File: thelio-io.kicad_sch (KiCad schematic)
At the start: 24 parts, among them Y1 16MHz

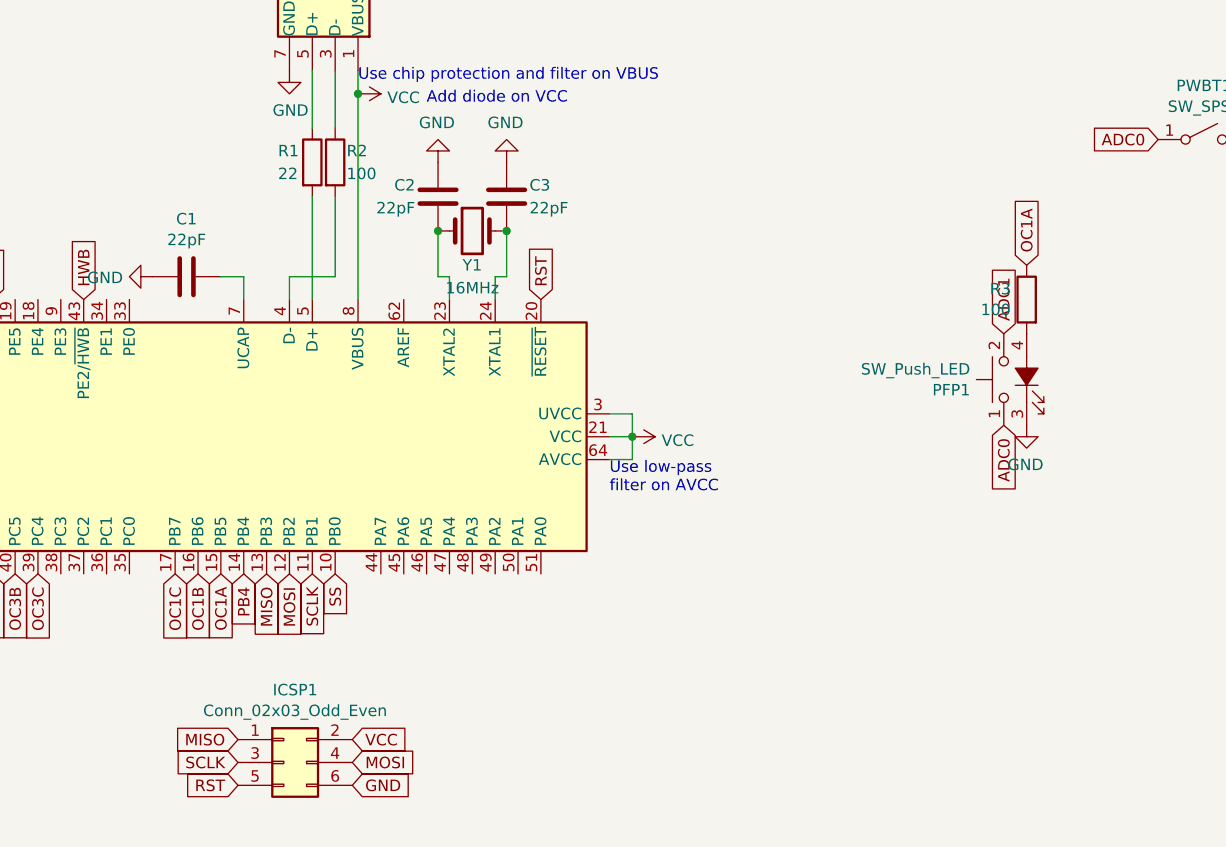
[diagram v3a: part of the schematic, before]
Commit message: decoupling, etc add 3x 1 uF decoupling caps change UCAP from 22 pF to 1 uF as required by AVR datasheet R3 0201 to 0603 package R2 100 to 22 ohm add part number for crystal move VCC planelet to In1.Cu, make In2.Cu solid plane layer swap some traces to allow for planes move power, ground vias closer to IC pins
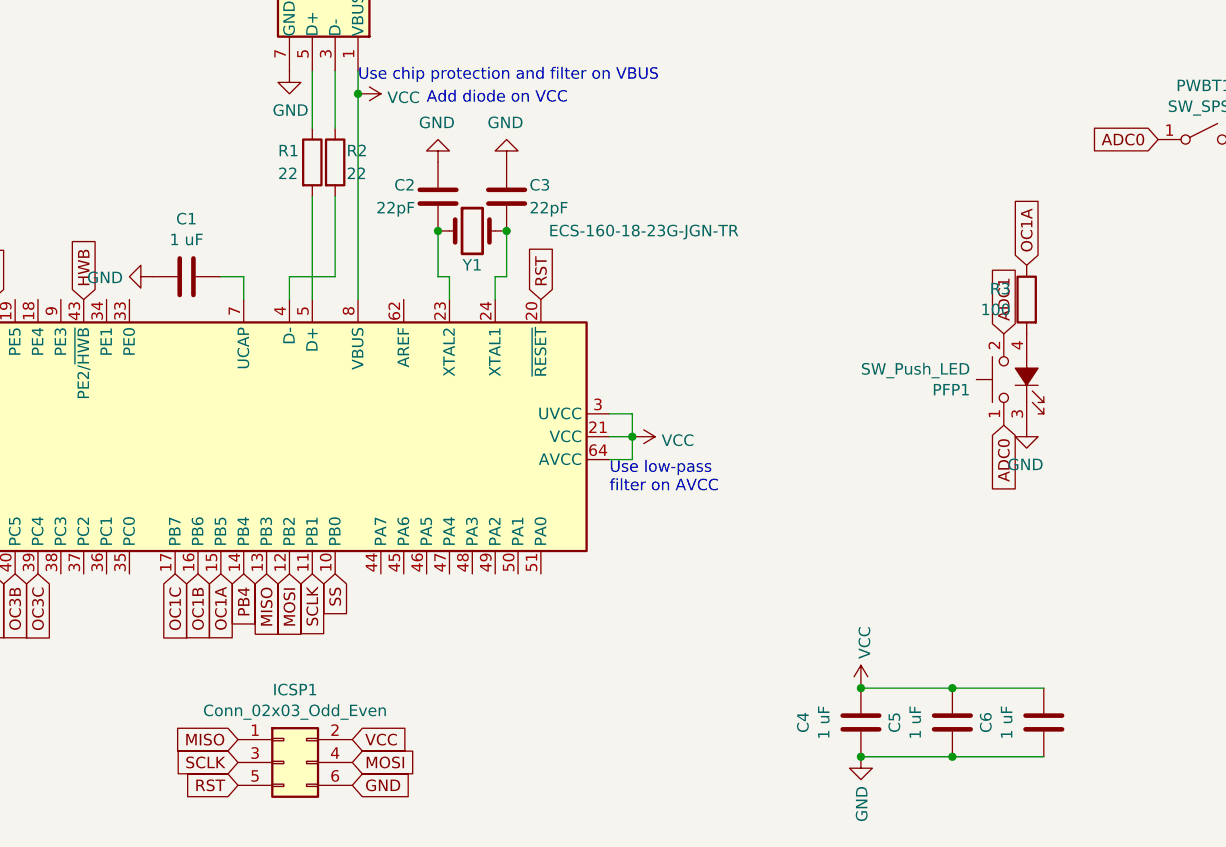
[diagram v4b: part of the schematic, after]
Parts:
- added C4, C5, C6: 1 uF, Capacitor_SMD:C_0402_1005Metric, symbol Device:C
- C1: value 22pF -> 1 uF
- R2: value 100 -> 22
- R3: footprint Resistor_SMD:R_0201_0603Metric -> Resistor_SMD:R_0603_1608Metric
- Y1: value 16MHz -> ECS-160-18-23G-JGN-TR
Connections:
- net GND: now also C4.2, C5.2, C6.2
- net VCC: now also C4.1, C5.1, C6.1
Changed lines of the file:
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@@
 (kicad_sch (version 20211123) (generator eeschema)
   (paper "A4")
+  (junction (at 172.72 154.94) (diameter 0) (color 0 0 0 0)
+  )
+  (junction (at 172.72 147.32) (diameter 0) (color 0 0 0 0)
+  )
   (junction (at 133.35 96.52) (diameter 0) (color 0 0 0 0)
   )
@@
   (junction (at 125.73 96.52) (diameter 0) (color 0 0 0 0)
   )
+  (junction (at 182.88 154.94) (diameter 0) (color 0 0 0 0)
+  )
+  (junction (at 182.88 147.32) (diameter 0) (color 0 0 0 0)
+  )
   (wire (pts (xy 104.14 104.14) (xy 104.14 101.6))
     (stroke (width 0) (type default) (color 0 0 0 0))
@@
     (stroke (width 0) (type default) (color 0 0 0 0))
   )
+  (wire (pts (xy 172.72 154.94) (xy 182.88 154.94))
+    (stroke (width 0) (type default) (color 0 0 0 0))
+  )
+  (wire (pts (xy 182.88 147.32) (xy 193.04 147.32))
+    (stroke (width 0) (type default) (color 0 0 0 0))
+  )
   (wire (pts (xy 111.76 92.71) (xy 111.76 104.14))
     (stroke (width 0) (type default) (color 0 0 0 0))
   )
+  (wire (pts (xy 172.72 147.32) (xy 182.88 147.32))
+    (stroke (width 0) (type default) (color 0 0 0 0))
+  )
   (wire (pts (xy 147.32 119.38) (xy 147.32 121.92))
     (stroke (width 0) (type default) (color 0 0 0 0))
@@
   )
   (wire (pts (xy 144.78 119.38) (xy 147.32 119.38))
+    (stroke (width 0) (type default) (color 0 0 0 0))
+  )
+  (wire (pts (xy 182.88 154.94) (xy 193.04 154.94))
     (stroke (width 0) (type default) (color 0 0 0 0))
   )
@@
     (pin "7")
     (pin "8")
+  )
+  (symbol (lib_id "power:GND") (at 172.72 154.94 0) (unit 1)
+    (in_bom yes) (on_board yes)
+    (property "Reference" "#PWR0101" (id 0) (at 172.72 161.29 0)
+      (effects (font (size 1.27 1.27)) hide)
+    )
+    (property "Value" "GND" (id 1) (at 172.847 158.1912 90)
+      (effects (font (size 1.27 1.27)) (justify right))
+    )
+    (property "Footprint" "" (id 2) (at 172.72 154.94 0)
+      (effects (font (size 1.27 1.27)) hide)
+    )
+    (property "Datasheet" "" (id 3) (at 172.72 154.94 0)
+      (effects (font (size 1.27 1.27)) hide)
+    )
+    (pin "1")
   )
   (symbol (lib_id "power:+12V") (at 266.065 54.61 270) (unit 1)
@@
     (pin "1")
   )
+  (symbol (lib_id "Device:C") (at 193.04 151.13 0) (unit 1)
+    (in_bom yes) (on_board yes)
+    (property "Reference" "C6" (id 0) (at 186.6392 151.13 90))
+    (property "Value" "1 uF" (id 1) (at 188.9506 151.13 90))
+    (property "Footprint" "Capacitor_SMD:C_0402_1005Metric" (id 2) (at 194.0052 154.94 0)
+      (effects (font (size 1.27 1.27)) hide)
+    )
+    (property "Datasheet" "~" (id 3) (at 193.04 151.13 0)
+      (effects (font (size 1.27 1.27)) hide)
+    )
+    (pin "1")
+    (pin "2")
+  )
   (symbol (lib_id "Connector_Generic:Conn_02x03_Odd_Even") (at 108.585 155.575 0) (unit 1)
     (in_bom yes) (on_board yes)
@@
       (effects (font (size 1.27 1.27)) (justify left))
     )
-    (property "Value" "100" (id 1) (at 115.57 90.17 0)
+    (property "Value" "22" (id 1) (at 115.57 90.17 0)
       (effects (font (size 1.27 1.27)) (justify left))
     )
@@
     (in_bom yes) (on_board yes)
     (property "Reference" "C1" (id 0) (at 97.79 95.1992 90))
-    (property "Value" "22pF" (id 1) (at 97.79 97.5106 90))
+    (property "Value" "1 uF" (id 1) (at 97.79 97.5106 90))
     (property "Footprint" "Capacitor_SMD:C_0402_1005Metric" (id 2) (at 93.98 102.5652 0)
       (effects (font (size 1.27 1.27)) hide)
@@
     (pin "2")
   )
+  (symbol (lib_id "power:VCC") (at 172.72 147.32 0) (unit 1)
+    (in_bom yes) (on_board yes)
+    (property "Reference" "#PWR0102" (id 0) (at 172.72 151.13 0)
+      (effects (font (size 1.27 1.27)) hide)
+    )
+    (property "Value" "VCC" (id 1) (at 173.1518 144.0688 90)
+      (effects (font (size 1.27 1.27)) (justify left))
+    )
+    (property "Footprint" "" (id 2) (at 172.72 147.32 0)
+      (effects (font (size 1.27 1.27)) hide)
+    )
+    (property "Datasheet" "" (id 3) (at 172.72 147.32 0)
+      (effects (font (size 1.27 1.27)) hide)
+    )
+    (pin "1")
+  )
+  (symbol (lib_id "Device:C") (at 172.72 151.13 0) (unit 1)
+    (in_bom yes) (on_board yes)
+    (property "Reference" "C4" (id 0) (at 166.3192 151.13 90))
+    (property "Value" "1 uF" (id 1) (at 168.6306 151.13 90))
+    (property "Footprint" "Capacitor_SMD:C_0402_1005Metric" (id 2) (at 173.6852 154.94 0)
+      (effects (font (size 1.27 1.27)) hide)
+    )
+    (property "Datasheet" "~" (id 3) (at 172.72 151.13 0)
+      (effects (font (size 1.27 1.27)) hide)
+    )
+    (pin "1")
+    (pin "2")
+  )
   (symbol (lib_id "Device:R") (at 191.135 104.14 0) (mirror y) (unit 1)
     (in_bom yes) (on_board yes)
@@
       (effects (font (size 1.27 1.27)) (justify left))
     )
-    (property "Footprint" "Resistor_SMD:R_0201_0603Metric" (id 2) (at 192.913 104.14 90)
+    (property "Footprint" "Resistor_SMD:R_0603_1608Metric" (id 2) (at 192.913 104.14 90)
       (effects (font (size 1.27 1.27)) hide)
     )
@@
     (in_bom yes) (on_board yes)
     (property "Reference" "Y1" (id 0) (at 129.54 100.33 0))
-    (property "Value" "16MHz" (id 1) (at 129.54 102.87 0))
+    (property "Value" "ECS-160-18-23G-JGN-TR" (id 1) (at 148.59 96.52 0))
     (property "Footprint" "Crystal:Crystal_SMD_0603-2Pin_6.0x3.5mm" (id 2) (at 129.54 96.52 0)
       (effects (font (size 1.27 1.27)) hide)
     )
     (property "Datasheet" "~" (id 3) (at 129.54 96.52 0)
+      (effects (font (size 1.27 1.27)) hide)
+    )
+    (pin "1")
+    (pin "2")
+  )
+  (symbol (lib_id "Device:C") (at 182.88 151.13 0) (unit 1)
+    (in_bom yes) (on_board yes)
+    (property "Reference" "C5" (id 0) (at 176.4792 151.13 90))
+    (property "Value" "1 uF" (id 1) (at 178.7906 151.13 90))
+    (property "Footprint" "Capacitor_SMD:C_0402_1005Metric" (id 2) (at 183.8452 154.94 0)
+      (effects (font (size 1.27 1.27)) hide)
+    )
+    (property "Datasheet" "~" (id 3) (at 182.88 151.13 0)
       (effects (font (size 1.27 1.27)) hide)
     )
@@
       (reference "#PWR023") (unit 1) (value "+12V") (footprint "")
     )
+    (path "/28d843b2-978b-4d39-bd30-26580fa80b83"
+      (reference "#PWR0101") (unit 1) (value "GND") (footprint "")
+    )
+    (path "/a2f6d203-ebeb-4775-ac27-92e1a315ea1f"
+      (reference "#PWR0102") (unit 1) (value "VCC") (footprint "")
+    )
     (path "/3a0f81ba-204f-45e9-83fb-f7bade0d2ad1"
       (reference "AVR1") (unit 1) (value "ATmega32U4-AU") (footprint "Package_DFN_QFN:QFN-64-1EP_9x9mm_P0.5mm_EP7.5x7.5mm")
     )
     (path "/95d7b4e4-d090-4b4b-95d7-0687255342ed"
-      (reference "C1") (unit 1) (value "22pF") (footprint "Capacitor_SMD:C_0402_1005Metric")
+      (reference "C1") (unit 1) (value "1 uF") (footprint "Capacitor_SMD:C_0402_1005Metric")
     )
     (path "/ca6b3c6e-f279-44df-940f-3fcf5357fcd4"
@@
       (reference "C3") (unit 1) (value "22pF") (footprint "Capacitor_SMD:C_0402_1005Metric")
     )
+    (path "/a878a433-44b7-4c70-8fb4-32bc0d732a65"
+      (reference "C4") (unit 1) (value "1 uF") (footprint "Capacitor_SMD:C_0402_1005Metric")
+    )
+    (path "/fc80f10e-2697-49ce-b85e-a5592bbe3889"
+      (reference "C5") (unit 1) (value "1 uF") (footprint "Capacitor_SMD:C_0402_1005Metric")
+    )
+    (path "/519c6cbc-2cef-4756-9976-f1eb263c94ab"
+      (reference "C6") (unit 1) (value "1 uF") (footprint "Capacitor_SMD:C_0402_1005Metric")
+    )
     (path "/684a5de3-a519-44ea-bebe-5a3b8e01f198"
       (reference "F1") (unit 1) (value "3A Fuse") (footprint "Fuse:Fuse_0603_1608Metric")
@@
     )
     (path "/5e98e7b2-f6af-4d33-bd91-1e12cd43a4af"
-      (reference "R2") (unit 1) (value "100") (footprint "Resistor_SMD:R_0603_1608Metric")
+      (reference "R2") (unit 1) (value "22") (footprint "Resistor_SMD:R_0603_1608Metric")
     )
     (path "/a93da457-a261-4a8a-92cf-b2b33bf2aef6"
-      (reference "R3") (unit 1) (value "100") (footprint "Resistor_SMD:R_0201_0603Metric")
+      (reference "R3") (unit 1) (value "100") (footprint "Resistor_SMD:R_0603_1608Metric")
     )
     (path "/24da91e1-4b2d-4e79-a096-b2424715c2dc"
@@
     )
     (path "/ee06c0cd-13b9-4549-a21e-0082e6f6e36d"
-      (reference "Y1") (unit 1) (value "16MHz") (footprint "Crystal:Crystal_SMD_0603-2Pin_6.0x3.5mm")
-    )
-  )
+      (reference "Y1") (unit 1) (value "ECS-160-18-23G-JGN-TR") (footprint "Crystal:Crystal_SMD_0603-2Pin_6.0x3.5mm")
+    )
+  )

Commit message: part numbers, export settings
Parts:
- added C8: 1 uF, Capacitor_SMD:C_0402_1005Metric, symbol Device:C
- AVR1: value ATmega32U4-AU -> AT90USB646-MUR; Manufacturer (none) -> Microchip
- C1, C4, C5, C6, R1, R2, R3: Manufacturer (none) -> generic
- C2, C3: value 22pF -> 22 pF; Manufacturer (none) -> generic
- F1: value 3A Fuse -> FMC16302WBTPCT; Manufacturer (none) -> Kamaya
- FANIN1, FANOUT1, FANOUT2, FANOUT3, FANOUT4: value Fan_Tacho_PWM -> 47053-1000; Manufacturer (none) -> Molex (generic OK)
- ICSP1: value Conn_02x03_Odd_Even -> 54202-S0803LF; Manufacturer (none) -> Amphenol FCI (generic equivalent OK)
- MUX1, MUX2, MUX3, MUX4: value 74LVC2G157 -> SN74LVC2G157DCUR; Manufacturer (none) -> TI
- PFP1, PMB1: value SW_Push_LED -> 22-28-4040; Manufacturer (none) -> Molex (generic OK)
- POWER1: value ATA_FLOPPY_POWER_4 -> 171825-4; Manufacturer (none) -> Molex (generic OK)
- PWBT1: value SW_SPST -> TL3342F260QG; Manufacturer (none) -> E-Switch (generic equivalent OK)
- USB1: value USB_IDC -> header_9_USB; Manufacturer (none) -> generic
- Y1: Manufacturer (none) -> ECS
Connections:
- net HWB is gone; now on net GND: AVR1.43 (PE2/~{HWB})
- net GND: now also MUX1.7 (~{G}), MUX2.7 (~{G}), MUX3.7 (~{G}), MUX4.7 (~{G}), C8.1
- net XTAL2: now reaches AVR1.23 (XTAL2), C2.2, Y1.1
- net XTAL1: now reaches AVR1.24 (XTAL1), C3.2, Y1.2
- net AREF: now reaches AVR1.62 (AREF)
- net AREF: now also C8.2
- net UCAP: now reaches AVR1.7 (UCAP), C1.1
- net OC1B: no longer names the net of AVR1.16 (PB6)
- net PB4: no longer names the net of AVR1.14 (PB4)
- net SS: no longer names the net of AVR1.10 (PB0)
- no-connect marks 0 -> 41
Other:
- note added: "OC1B"
- note added: "SS"
- note removed: "Add diode on VCC"
- note removed: "Use chip protection and filter on VBUS"
- note removed: "Use low-pass filter on AVCC"
- company: (none) -> System76
- title: (none) -> Thelio IO
- moved on the sheet: AVR1, C1, C2, C3, ICSP1, R1, R2, USB1, Y1

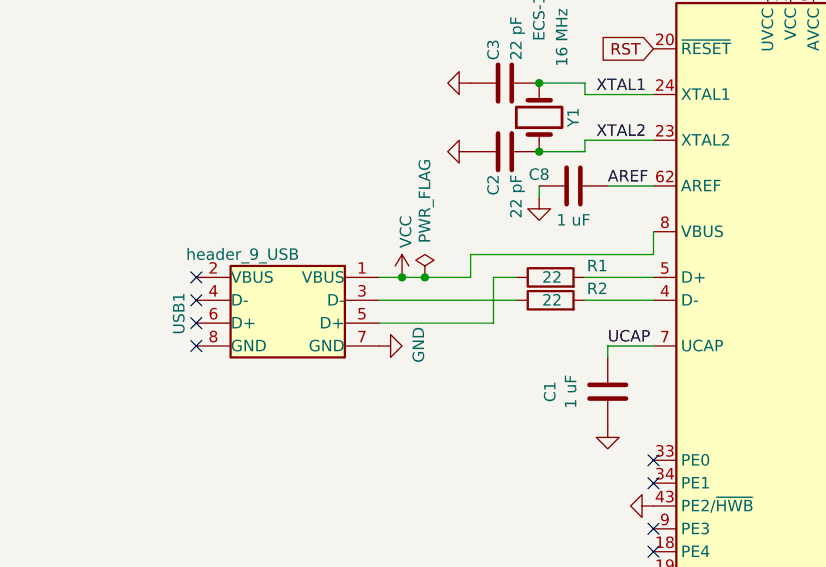
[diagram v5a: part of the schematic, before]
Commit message: change USB connector to Molex SL style
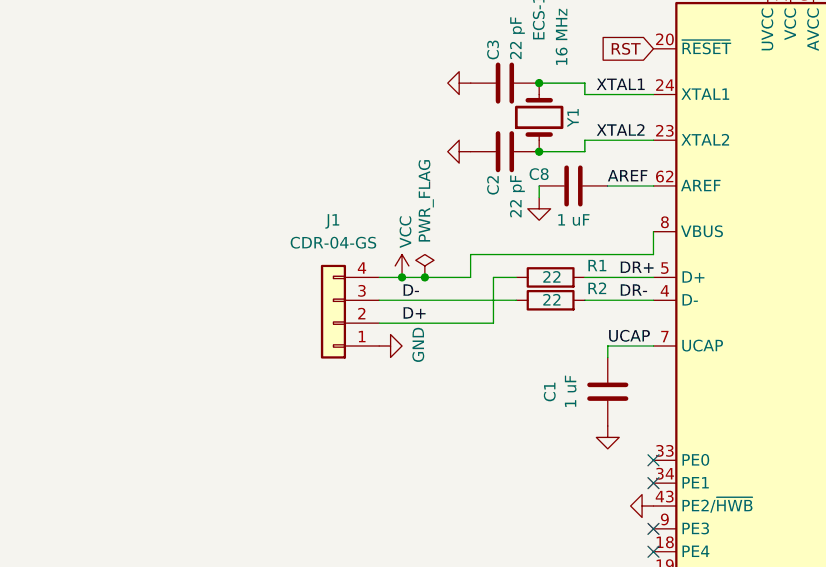
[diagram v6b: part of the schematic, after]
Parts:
- removed USB1: header_9_USB, USB:USB_IDC, symbol USB:USB_IDC
- added J1: CDR-04-GS, Connector_Molex:Molex_SL_171971-0004_1x04_P2.54mm_Vertical, symbol Connector_Generic:Conn_01x04
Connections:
- net GND: now also J1.1 (Pin_1)
- net VCC: now also J1.4 (Pin_4)
- net D+: now reaches R1.1
- net D+: now also J1.2 (Pin_2)
- net DR+: now reaches AVR1.5 (D+), R1.2
- net D-: now reaches R2.1
- net D-: now also J1.3 (Pin_3)
- net DR-: now reaches AVR1.4 (D-), R2.2
- no-connect marks 41 -> 37
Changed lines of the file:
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@@
   )
   (no_connect (at 128.27 91.44))
-  (no_connect (at 46.99 124.46))
   (no_connect (at 128.27 106.68))
   (no_connect (at 128.27 93.98))
@@
   (no_connect (at 158.115 54.61))
   (no_connect (at 128.27 142.24))
-  (no_connect (at 46.99 119.38))
   (no_connect (at 128.27 177.8))
   (no_connect (at 128.27 170.18))
-  (no_connect (at 46.99 116.84))
   (no_connect (at 203.2 39.37))
   (no_connect (at 128.27 124.46))
@@
   (no_connect (at 128.27 109.22))
   (no_connect (at 128.27 101.6))
-  (no_connect (at 46.99 121.92))
   (no_connect (at 128.27 154.94))
   (no_connect (at 128.27 99.06))
@@
     (effects (font (size 1.27 1.27)) (justify right bottom))
   )
+  (label "DR+" (at 93.98 116.84 0)
+    (effects (font (size 1.27 1.27)) (justify left bottom))
+  )
   (label "XTAL2" (at 91.44 101.6 0)
     (effects (font (size 1.27 1.27)) (justify left bottom))
@@
     (effects (font (size 1.27 1.27)) (justify left bottom))
   )
+  (label "DR-" (at 93.98 119.38 0)
+    (effects (font (size 1.27 1.27)) (justify left bottom))
+  )
   (label "XTAL1" (at 91.44 96.52 0)
+    (effects (font (size 1.27 1.27)) (justify left bottom))
+  )
+  (label "D+" (at 69.85 121.92 0)
+    (effects (font (size 1.27 1.27)) (justify left bottom))
+  )
+  (label "D-" (at 69.85 119.38 0)
     (effects (font (size 1.27 1.27)) (justify left bottom))
   )
@@
     )
     (pin "1")
-  )
-  (symbol (lib_id "USB:USB_IDC") (at 62.23 121.92 0) (mirror y) (unit 1)
-    (in_bom yes) (on_board yes)
-    (property "Reference" "USB1" (id 0) (at 45.085 123.19 90)
-      (effects (font (size 1.27 1.27)) (justify left))
-    )
-    (property "Value" "header_9_USB" (id 1) (at 58.42 114.3 0)
-      (effects (font (size 1.27 1.27)) (justify left))
-    )
-    (property "Footprint" "USB:USB_IDC" (id 2) (at 62.23 121.92 0)
-      (effects (font (size 1.27 1.27)) hide)
-    )
-    (property "Datasheet" "~" (id 3) (at 62.23 121.92 0)
-      (effects (font (size 1.27 1.27)) hide)
-    )
-    (property "Description" "10 pin shrouded 2x5 2.54 mm pitch header with pin 9 removed" (id 4) (at 62.23 121.92 0)
-      (effects (font (size 1.27 1.27)) hide)
-    )
-    (property "Manufacturer" "generic" (id 5) (at 62.23 121.92 0)
-      (effects (font (size 1.27 1.27)) hide)
-    )
-    (pin "1")
-    (pin "2")
-    (pin "3")
-    (pin "4")
-    (pin "5")
-    (pin "6")
-    (pin "7")
-    (pin "8")
   )
   (symbol (lib_id "power:GND") (at 172.72 154.94 0) (unit 1)
@@
     (pin "2")
   )
+  (symbol (lib_id "Connector_Generic:Conn_01x04") (at 62.23 121.92 180) (unit 1)
+    (in_bom yes) (on_board yes) (fields_autoplaced)
+    (property "Reference" "J1" (id 0) (at 62.23 110.49 0))
+    (property "Value" "CDR-04-GS" (id 1) (at 62.23 113.03 0))
+    (property "Footprint" "Connector_Molex:Molex_SL_171971-0004_1x04_P2.54mm_Vertical" (id 2) (at 62.23 121.92 0)
+      (effects (font (size 1.27 1.27)) hide)
+    )
+    (property "Datasheet" "~" (id 3) (at 62.23 121.92 0)
+      (effects (font (size 1.27 1.27)) hide)
+    )
+    (property "Description" "Molex SL type 4 pin header" (id 4) (at 62.23 121.92 0)
+      (effects (font (size 1.27 1.27)) hide)
+    )
+    (property "Manufacturer" "Adam Tech" (id 5) (at 62.23 121.92 0)
+      (effects (font (size 1.27 1.27)) hide)
+    )
+    (pin "1")
+    (pin "2")
+    (pin "3")
+    (pin "4")
+  )
   (symbol (lib_id "Connector_Generic:Conn_02x03_Odd_Even") (at 152.4 182.88 0) (unit 1)
     (in_bom yes) (on_board yes)
@@
       (reference "ICSP1") (unit 1) (value "54202-S0803LF") (footprint "Connector_PinHeader_2.54mm:PinHeader_2x03_P2.54mm_Vertical_SMD")
     )
+    (path "/51ae0665-cd2b-4e70-8e0e-7ee01f95204e"
+      (reference "J1") (unit 1) (value "CDR-04-GS") (footprint "Connector_Molex:Molex_SL_171971-0004_1x04_P2.54mm_Vertical")
+    )
     (path "/6026c5cd-21a3-4f20-a47c-7421b97b08a8"
       (reference "MUX1") (unit 1) (value "SN74LVC2G157DCUR") (footprint "Package_SO:VSSOP-8_2.4x2.1mm_P0.5mm")
@@
       (reference "R3") (unit 1) (value "100") (footprint "Resistor_SMD:R_0603_1608Metric")
     )
-    (path "/24da91e1-4b2d-4e79-a096-b2424715c2dc"
-      (reference "USB1") (unit 1) (value "header_9_USB") (footprint "USB:USB_IDC")
-    )
     (path "/ee06c0cd-13b9-4549-a21e-0082e6f6e36d"
